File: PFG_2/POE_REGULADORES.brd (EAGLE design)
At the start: 111.7 x 95.9 mm, 185 parts, among them J1 1-406541-1, J10 OSTVN04A150, J2 AMPS_Connect, J3 Port Current, J4 OSTVN04A150, J5 TB001-500-02BE, J6 OSTVN02A150, J7 OSTVN02A150, J8 TB001-500-02BE, J9 TB001-500-02BE, Q1 FDN8601, Q2 FDN8601, Q3 FDN8601, Q4 FDN8601, Q5 CSD18533Q5A, Q6 CSD18533Q5A, T1 750313355, U1 7490220122, U10 12V, U11 FCX493TA, U12 TL431AIDBVR, U13 LM5165DRCR, U14 ENC28J60-I/SP, U2 TPS2373-3RGWT, U3 UCC2897APW, U4 12V, U5 FCX493TA, U6 TCMT1107, U7 MMBT3906, U8 FDMS86250, U9 IRFR9220PBF, Y1 Crystal_25Mhz

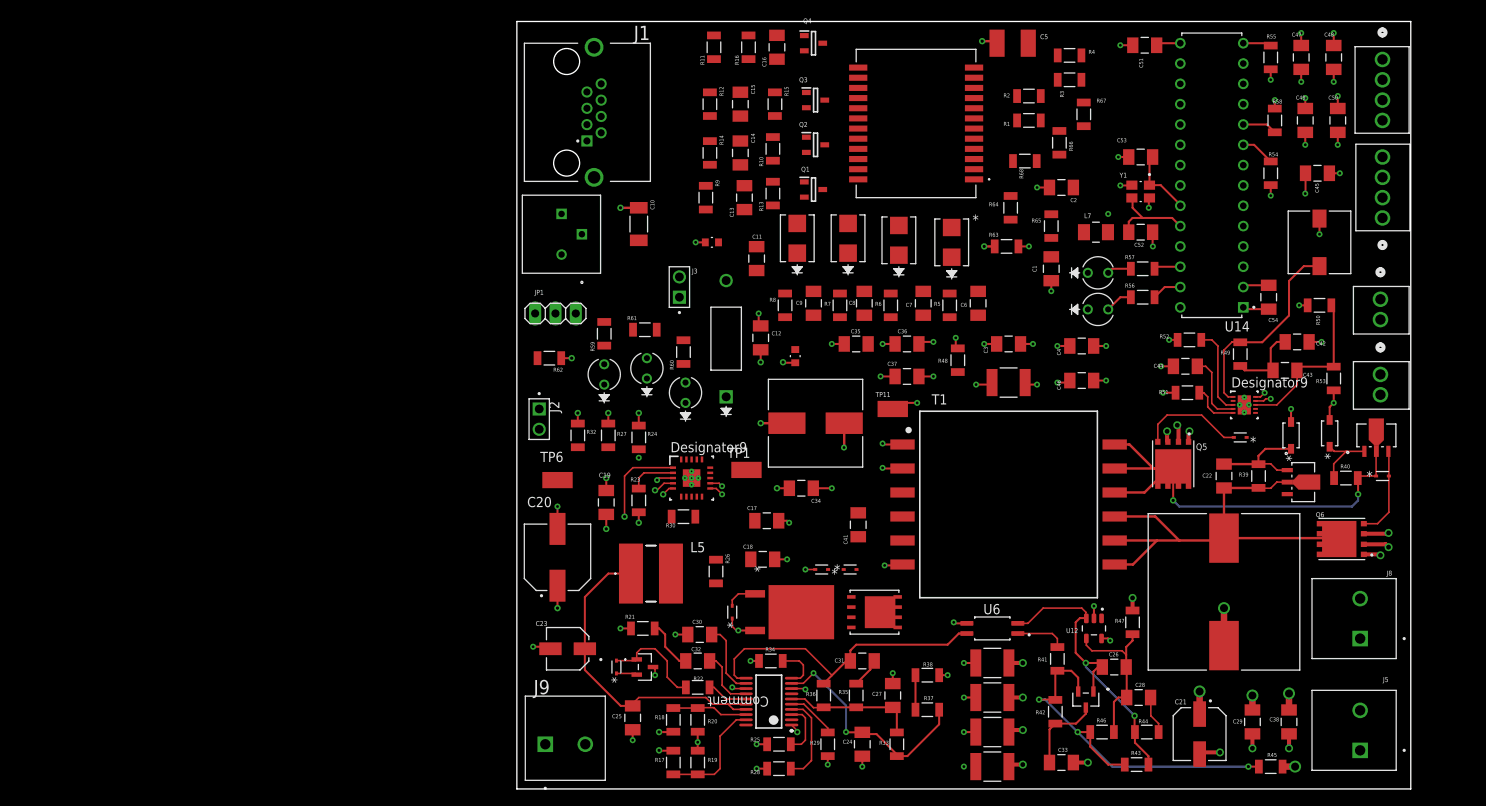
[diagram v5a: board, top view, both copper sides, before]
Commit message: Falta vias de conector poe y transformador TPS23
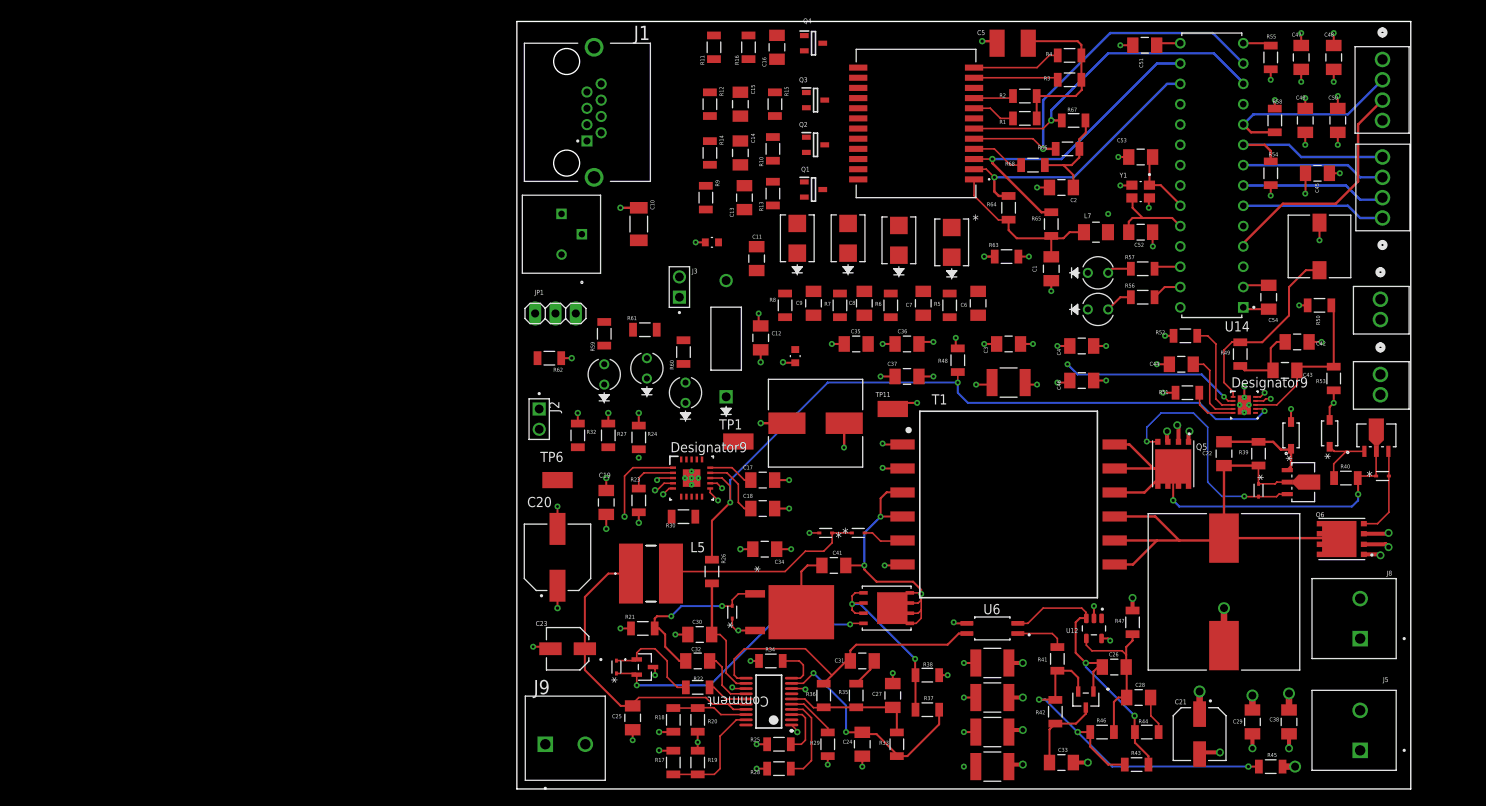
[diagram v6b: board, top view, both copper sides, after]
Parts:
- moved C34 8.89 mm to (31.0, 30.0)
- moved D8 6.99 mm to (92.7, 37.3), turned to 270 degrees
- moved C18 6.35 mm to (30.7, 35.1)
- moved C41 5.92 mm to (39.6, 27.9), turned to 0 degrees
- moved C17 5.11 mm to (30.7, 38.6)
- moved D10 4.68 mm to (42.7, 32.0)
- moved D11 4.60 mm to (38.6, 32.0)
- moved TP1 3.70 mm to (27.7, 43.4)
- moved C22 2.79 mm to (88.4, 41.9)
- moved R39 2.79 mm to (92.7, 41.9)
- moved U8 1.61 mm to (46.2, 22.6)
- moved R67 1.48 mm to (69.6, 83.6), turned to 0 degrees
- moved R66 1.27 mm to (68.8, 80.0), turned to 0 degrees
- moved R63 1.27 mm to (61.2, 66.5)
- moved R68 1.14 mm to (64.5, 78.0)
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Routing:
- net PG: track 0.00 -> 93.3 mm, vias 0 -> 3
- net RXD_P: track 0.00 -> 46.9 mm, vias 0 -> 1
- net RXD_N: track 0.00 -> 41.3 mm, vias 0 -> 1
- net TXD_N: track 0.00 -> 41.1 mm, vias 0 -> 1
- net N$59: track 0.00 -> 35.9 mm, vias 0 -> 3
- net TXD_P: track 0.00 -> 34.8 mm, vias 0 -> 1
- net N$60: track 2.60 -> 35.5 mm, vias 0 -> 2
- net N_INT: track 0.00 -> 29.4 mm
- net N$55: track 0.00 -> 26.1 mm
- net VDD_P: track 23.5 -> 46.1 mm, vias 11 -> 13
- net TXD_CT: track 0.00 -> 21.9 mm
- net N$17: track 0.00 -> 21.3 mm
- net RESET_ETH: track 4.34 -> 24.1 mm
- net N$54: track 4.32 -> 23.5 mm, vias 0 -> 2
- net CS: track 4.29 -> 23.1 mm
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
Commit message: Finalizado el enrutado y resueltos errores DCR
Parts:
- moved R30 30.7 mm to (13.0, 63.8), turned to 270 degrees
- moved C6 22.9 mm to (34.8, 60.7)
- moved R8 21.6 mm to (55.1, 61.0), turned to 270 degrees
- moved C9 21.6 mm to (58.7, 60.7)
- moved D4 20.3 mm to (55.4, 68.8), turned to 270 degrees
- moved D1 18.3 mm to (36.1, 68.6), turned to 270 degrees
- moved R5 15.5 mm to (38.6, 60.7), turned to 270 degrees
- moved TP11 13.0 mm to (40.4, 36.3)
- moved C16 10.9 mm to (21.6, 92.7)
- moved R12 9.37 mm to (30.2, 92.7)
- moved C19 8.67 mm to (2.54, 36.6)
- moved C8 8.65 mm to (52.1, 61.2)
- moved R7 8.14 mm to (48.5, 61.0), turned to 270 degrees
- moved R11 7.90 mm to (30.2, 87.1), turned to 270 degrees
- moved C13 6.90 mm to (21.6, 74.7), turned to 270 degrees
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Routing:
- net N$36: track 0.00 -> 110.4 mm
- net PR78: track 0.00 -> 64.0 mm, vias 0 -> 3
- net PR36: track 0.00 -> 60.0 mm, vias 0 -> 3
- net N$30: track 0.00 -> 53.4 mm
- net PR45: track 0.00 -> 46.9 mm, vias 0 -> 2
- net N$15: track 0.00 -> 45.1 mm, vias 0 -> 2
- net MPS_DUTY: track 0.00 -> 44.9 mm, vias 0 -> 1
- net PR12: track 0.00 -> 40.6 mm, vias 0 -> 2
- net N$7: track 0.00 -> 37.0 mm, vias 0 -> 1
- net N$5: track 0.00 -> 35.7 mm, vias 0 -> 1
- net N$1: track 0.00 -> 35.4 mm, vias 0 -> 1
- net N$8: track 0.00 -> 35.3 mm, vias 0 -> 1
- net N$6: track 0.00 -> 35.0 mm, vias 0 -> 2
- net N$3: track 0.00 -> 34.6 mm, vias 0 -> 1
- net N$4: track 0.00 -> 34.0 mm, vias 0 -> 1
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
